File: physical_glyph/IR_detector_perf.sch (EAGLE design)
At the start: 31 parts, among them IC1 7805T, T1 BP103, U1 MCP6004-I/P, U2 LM339PWR

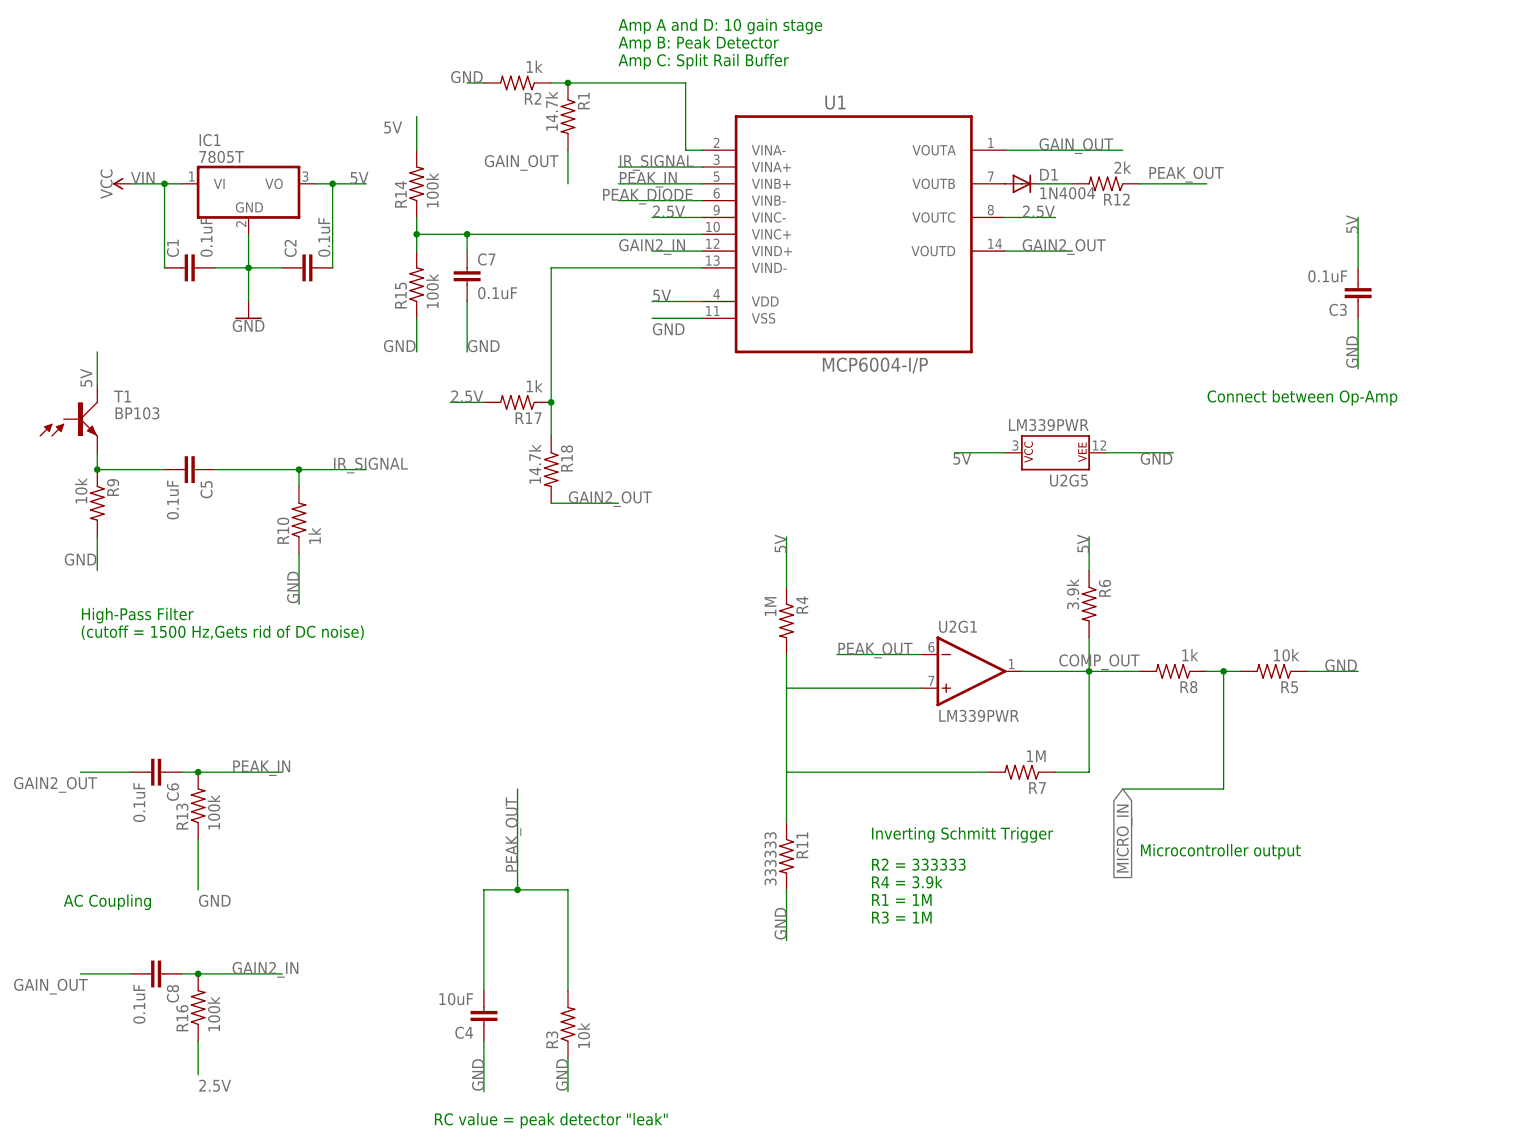
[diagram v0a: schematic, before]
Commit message: Simplify all resistors and clarify comparator resistors
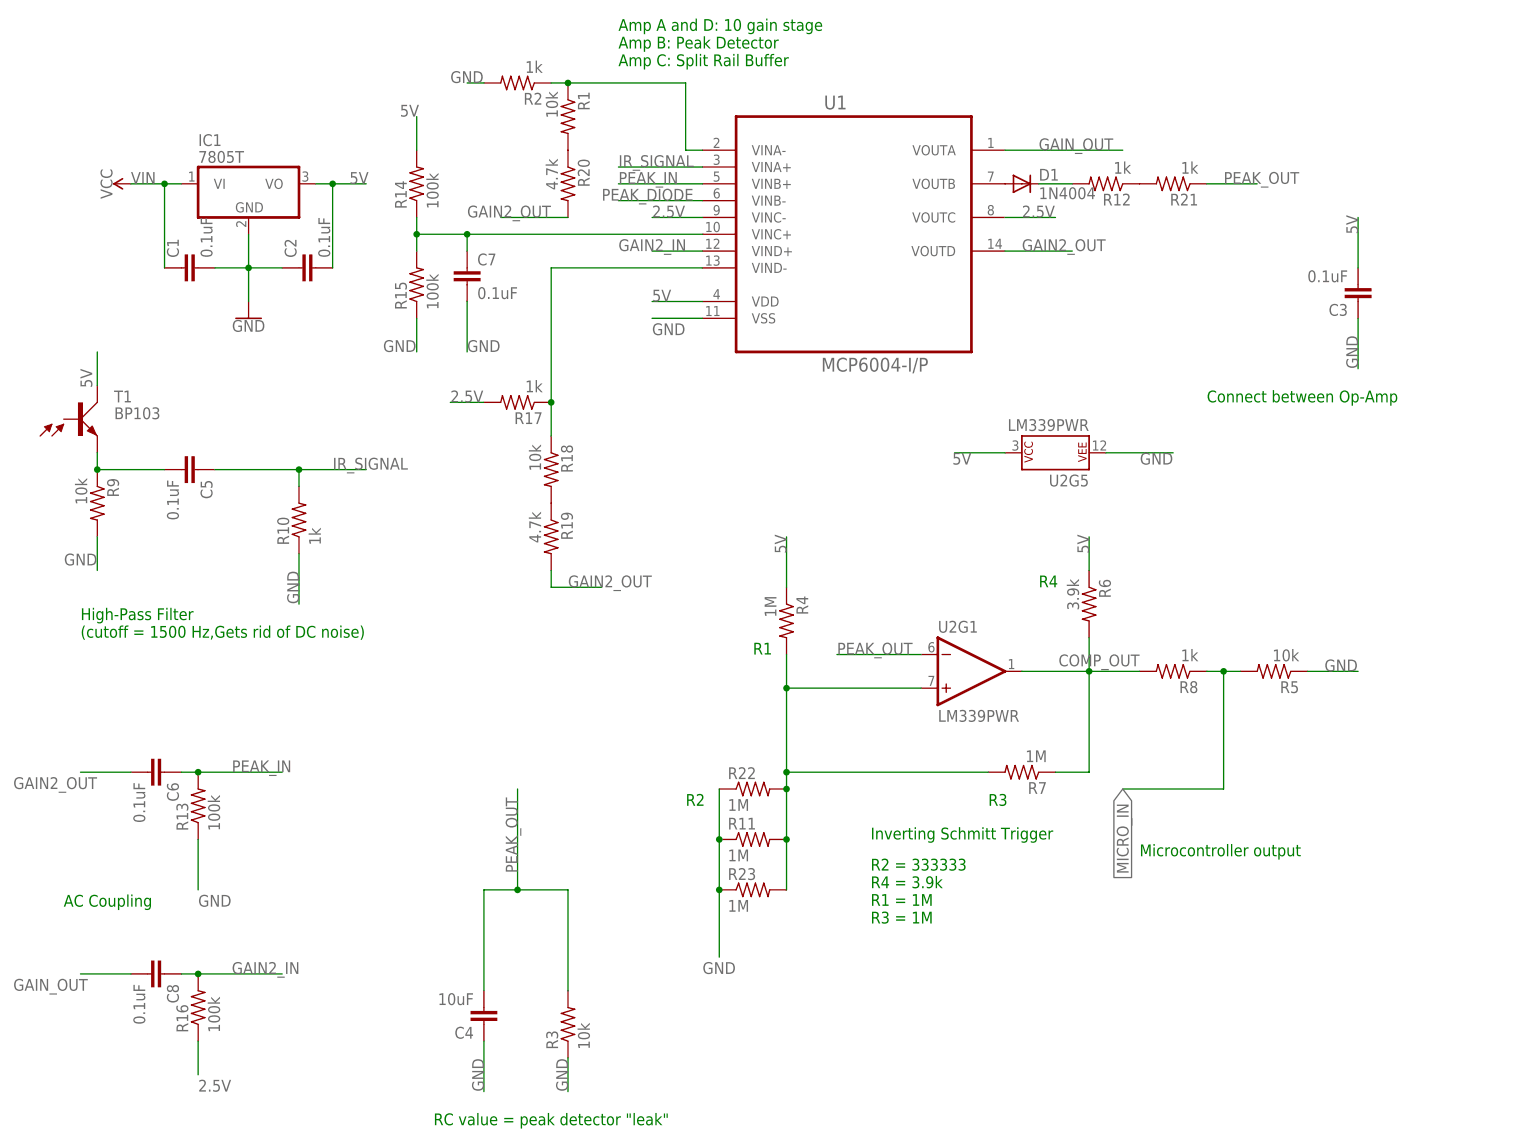
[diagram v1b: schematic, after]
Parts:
- added R19, R20: 4.7k, rcl:R-US_0204/2V
- added R21: 1k, rcl:R-US_0204/2V
- added R22, R23: 1M, rcl:R-US_0204/2V
- R1, R18: value 14.7k -> 10k
- R11: value 333333 -> 1M
- R12: value 2k -> 1k
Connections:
- new net N$6: R18.2, R19.1
- new net N$7: R1.2, R20.1
- new net N$8: R12.1, R21.2
- net GAIN2_OUT: now also R19.2, R20.2; no longer R18.2
- net GAIN_OUT: no longer R1.2
- net GND: now also R11.1, R22.1, R23.1; no longer R11.2
- net N$34: now also R11.2, R22.2, R23.2; no longer R11.1
- net PEAK_OUT: now also R21.1; no longer R12.1
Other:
- note added: "R1"
- note added: "R2"
- note added: "R3"
- note added: "R4"
- moved on the sheet: R11

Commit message: Final edits and fixes to IR detector circuit
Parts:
- added C9: 0.1uF, resistor:C-EU025-024X044
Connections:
- net 5V: now also C9.2
- net GAIN2_OUT: no longer R20.2
- net GAIN_OUT: now also R20.2
- net GND: now also C9.1
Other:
- note added: "Amp A and D: 14.7 gain stage Amp B: Peak Detector Amp C: Split Rail Buffer"
- note added: "Package option used here is TSSOP but I am using DIP"
- note added: "Stabilizing resistor for peak detector"
- note removed: "Amp A and D: 10 gain stage Amp B: Peak Detector Amp C: Split Rail Buffer"
- note removed: "Connect between Op-Amp"
- moved on the sheet: C3, R12, R21
